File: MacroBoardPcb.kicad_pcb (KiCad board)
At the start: 2 copper layers, 101.4 x 54.7 mm, 35 parts, among them J1 AVR-ISP-6, SW1 SW_Push, SW2 Rotary_Encoder_Switch, U1 ATmega32U4-AU, Y1 16MHz

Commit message: finished with small modifications
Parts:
- moved USB1 1.03 mm to (111.7, 82.2)
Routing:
- net D-: track 6.60 -> 7.88 mm
- net +5V: track 167.0 -> 168.0 mm
- net Net-(R2-Pad2): track 8.54 -> 9.57 mm
- net Net-(R1-Pad2): track 8.37 -> 9.40 mm
- net D+: track 7.67 -> 8.70 mm
- net GND: track 295.5 -> 294.9 mm
- net ANALOG: track 64.4 -> 63.9 mm, vias 0 -> 2
- net COL3: track 97.8 -> 97.9 mm, vias 0 -> 2
- net S0: vias 1 -> 4
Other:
- board size 101.4 x 54.7 mm -> 98.9 x 54.7 mm
- board text added: "Mboard Pcb"

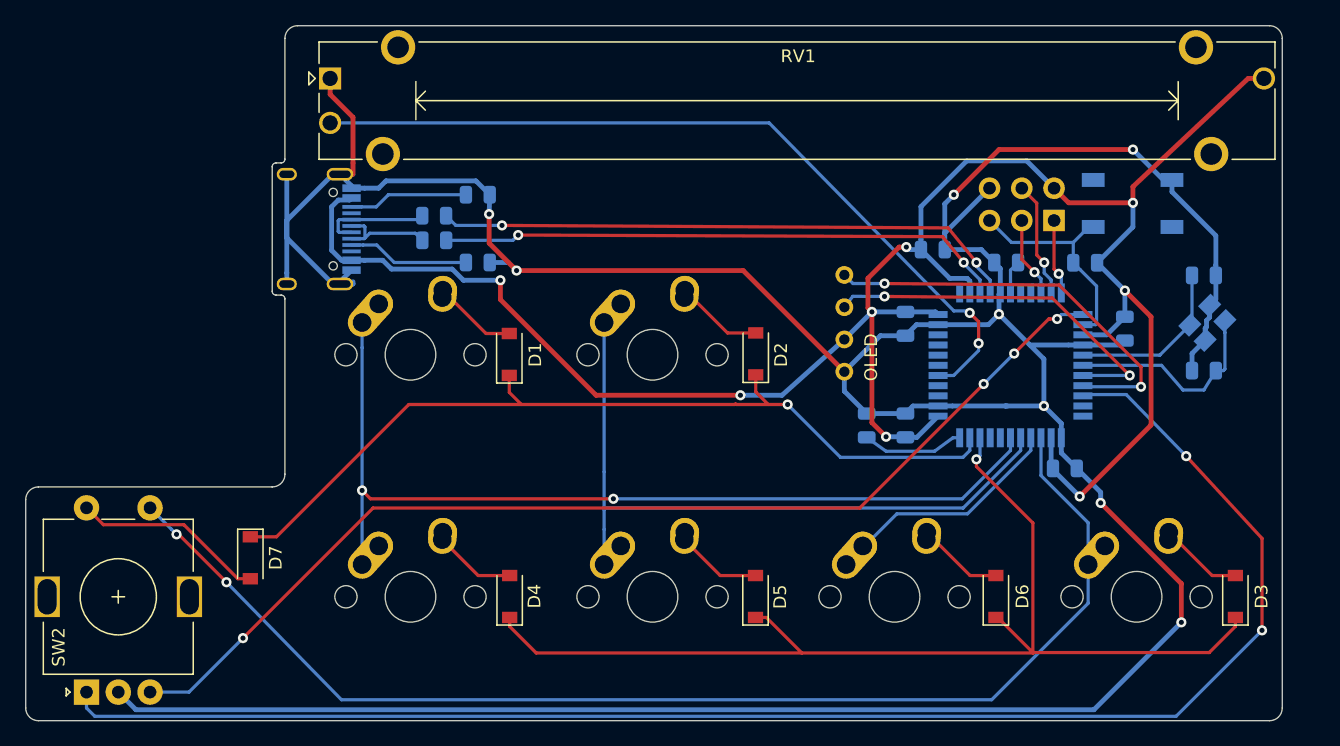
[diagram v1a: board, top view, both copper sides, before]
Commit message: added ground fills
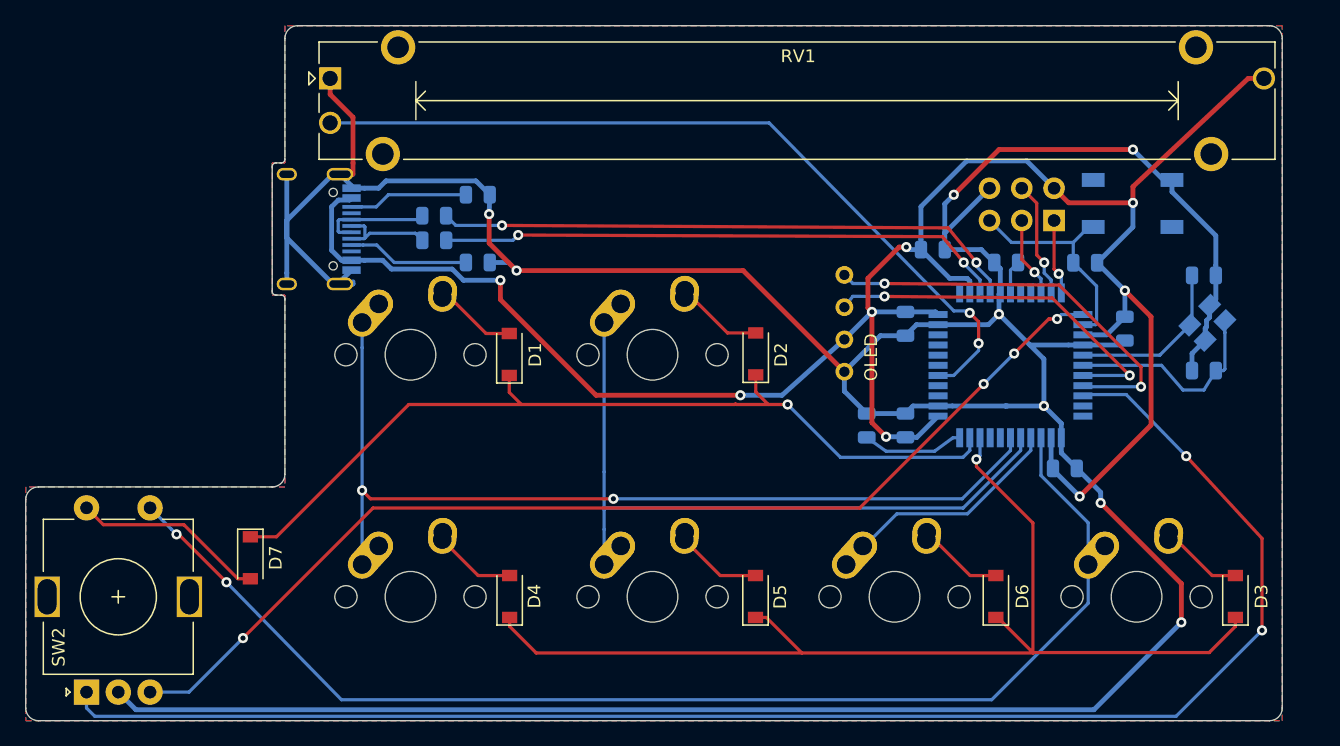
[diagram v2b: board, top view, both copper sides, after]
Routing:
- added copper zone on B.Cu, net GND
- added copper zone on F.Cu, net GND
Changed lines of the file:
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@@
   (segment (start 105.731969 106.231969) (end 105.568031 106.231969) (width 0.254) (layer F.Cu) (net 34))
   (segment (start 109.5 110) (end 105.731969 106.231969) (width 0.254) (layer F.Cu) (net 34))
+  (zone (net 1) (net_name GND) (layer F.Cu) (hatch edge 0.508)
+    (connect_pads (clearance 0.508))
+    (min_thickness 0.254)
+    (fill yes (arc_segments 32) (thermal_gap 0.508) (thermal_bridge_width 0.508))
+    (polygon
+      (pts
+        (xy 93.7 120.9) (xy 192.6 120.9) (xy 192.6 66.2) (xy 114.1 66.2) (xy 114.1 77)
+        (xy 113.1 77) (xy 113.1 87.4) (xy 114.1 87.4) (xy 114.1 102.5) (xy 93.7 102.5)
+      )
+    )
+  )
+  (zone (net 1) (net_name GND) (layer B.Cu) (hatch edge 0.508)
+    (connect_pads (clearance 0.508))
+    (min_thickness 0.254)
+    (fill yes (arc_segments 32) (thermal_gap 0.508) (thermal_bridge_width 0.508))
+    (polygon
+      (pts
+        (xy 93.7 120.9) (xy 192.6 120.9) (xy 192.6 66.2) (xy 114.1 66.2) (xy 114.1 77)
+        (xy 113.1 77) (xy 113.1 87.4) (xy 114.1 87.4) (xy 114.1 102.5) (xy 93.7 102.5)
+      )
+    )
+  )
 )
